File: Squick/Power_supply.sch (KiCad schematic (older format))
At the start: 17 parts, among them J10 D24V3F-5V, J9 BATT, Q1 Q_PMOS_GSD, SW4 ON/OFF, U10 LM1117-3.3

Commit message: Fixed footprints and symbol
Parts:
- SW4: footprint Button_Switch_SMD:Tact_Switch_SMD_3x6mm -> Button_Switch_SMD:SW_SPDT_CK-JS102011SAQN
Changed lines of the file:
@@
 F 0 "SW4" H 2075 6585 50  0000 C CNN
 F 1 "ON/OFF" H 2075 6494 50  0000 C CNN
-F 2 "Button_Switch_SMD:Tact_Switch_SMD_3x6mm" H 2075 6300 50  0001 C CNN
+F 2 "Button_Switch_SMD:SW_SPDT_CK-JS102011SAQN" H 2075 6300 50  0001 C CNN
 F 3 "~" H 2075 6300 50  0001 C CNN
 	1    2075 6300

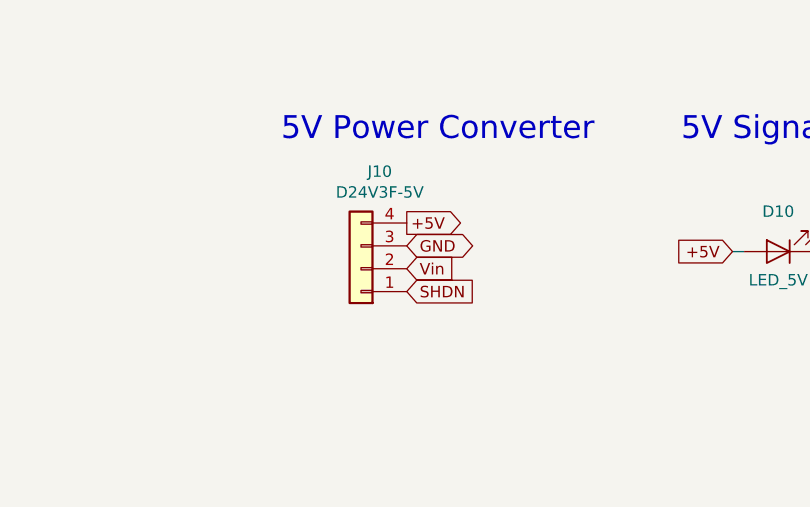
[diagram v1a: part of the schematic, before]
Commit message: Progress with PCB and some footprint debugs
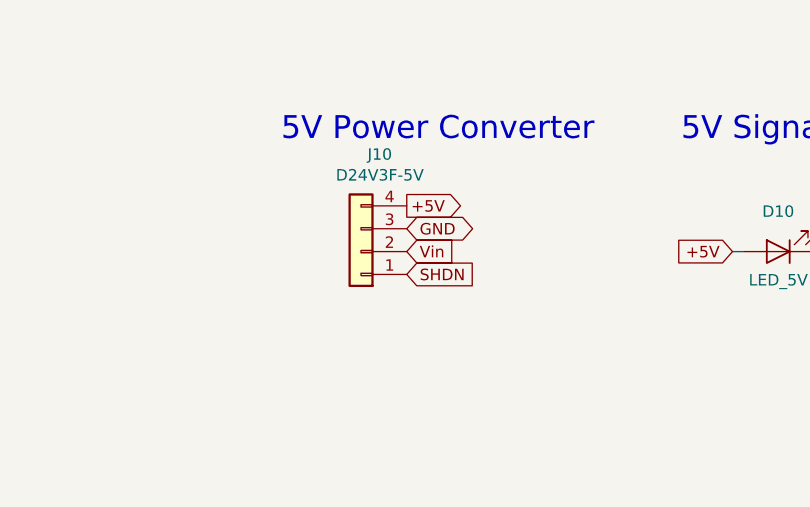
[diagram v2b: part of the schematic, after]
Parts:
- J10: footprint Connector_PinSocket_2.54mm:PinSocket_1x02_P2.54mm_Vertical -> Connector_PinSocket_2.54mm:PinSocket_1x04_P2.54mm_Vertical
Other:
- moved on the sheet: J10
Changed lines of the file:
@@
 	1    0    0    -1
 $EndComp
-Text GLabel 7100 2275 2    50   Input ~ 0
+Text GLabel 7100 2200 2    50   Input ~ 0
 SHDN
-Text GLabel 7100 2175 2    50   Input ~ 0
+Text GLabel 7100 2100 2    50   Input ~ 0
 Vin
-Text GLabel 7100 2075 2    50   BiDi ~ 0
+Text GLabel 7100 2000 2    50   BiDi ~ 0
 GND
 $Comp
 L Connector_Generic:Conn_01x04 J?
 U 1 1 60828861
-P 6900 2175
+P 6900 2100
 AR Path="/60828861" Ref="J?"  Part="1"
 AR Path="/608248A8/60828861" Ref="J10"  Part="1"
-F 0 "J10" H 6818 1750 50  0000 C CNN
-F 1 "D24V3F-5V" H 6818 1841 50  0000 C CNN
-F 2 "Connector_PinSocket_2.54mm:PinSocket_1x02_P2.54mm_Vertical" H 6900 2175 50  0001 C CNN
-F 3 "~" H 6900 2175 50  0001 C CNN
-	1    6900 2175
+F 0 "J10" H 6818 1675 50  0000 C CNN
+F 1 "D24V3F-5V" H 6818 1766 50  0000 C CNN
+F 2 "Connector_PinSocket_2.54mm:PinSocket_1x04_P2.54mm_Vertical" H 6900 2100 50  0001 C CNN
+F 3 "~" H 6900 2100 50  0001 C CNN
+	1    6900 2100
 	-1   0    0    1
 $EndComp
@@
 Wire Wire Line
 	2775 5525 2775 5625
-Text GLabel 7100 1975 2    50   Output ~ 0
+Text GLabel 7100 1900 2    50   Output ~ 0
 +5V
 $Comp

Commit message: Major progress with PCB design
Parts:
- C23, C26: footprint Capacitor_SMD:C_Elec_4x5.4 -> Capacitor_SMD:C_0603_1608Metric
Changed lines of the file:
@@
 F 0 "C23" H 6265 4796 50  0000 L CNN
 F 1 "100n" H 6265 4705 50  0000 L CNN
-F 2 "Capacitor_SMD:C_Elec_4x5.4" H 6188 4600 50  0001 C CNN
+F 2 "Capacitor_SMD:C_0603_1608Metric" H 6188 4600 50  0001 C CNN
 F 3 "~" H 6150 4750 50  0001 C CNN
 	1    6150 4750
@@
 F 0 "C26" H 8115 4771 50  0000 L CNN
 F 1 "100n" H 8115 4680 50  0000 L CNN
-F 2 "Capacitor_SMD:C_Elec_4x5.4" H 8038 4575 50  0001 C CNN
+F 2 "Capacitor_SMD:C_0603_1608Metric" H 8038 4575 50  0001 C CNN
 F 3 "~" H 8000 4725 50  0001 C CNN
 	1    8000 4725

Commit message: PCB project almost finished (without connections)
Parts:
- Q1: footprint (none) -> Package_TO_SOT_SMD:SOT-23
- R28: value 1.5k -> 10k; footprint Resistor_SMD:R_0805_2012Metric -> (none)
- SW4: value ON/OFF -> SW_SPDT; footprint Button_Switch_SMD:SW_SPDT_CK-JS102011SAQN -> (none)
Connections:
- net GND: now also R28.2; no longer R28.1
- net at Q1.1 (G): now also R28.1; no longer R28.2
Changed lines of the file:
@@
 $EndComp
-$Comp
-L Switch:SW_SPDT SW?
-U 1 1 60828874
-P 2075 6300
-AR Path="/60828874" Ref="SW?"  Part="1"
-AR Path="/608248A8/60828874" Ref="SW4"  Part="1"
-F 0 "SW4" H 2075 6585 50  0000 C CNN
-F 1 "ON/OFF" H 2075 6494 50  0000 C CNN
-F 2 "Button_Switch_SMD:SW_SPDT_CK-JS102011SAQN" H 2075 6300 50  0001 C CNN
-F 3 "~" H 2075 6300 50  0001 C CNN
-	1    2075 6300
-	-1   0    0    -1
-$EndComp
-$Comp
-L Device:Q_PMOS_GSD Q?
-U 1 1 6082887A
-P 2775 6200
-AR Path="/6082887A" Ref="Q?"  Part="1"
-AR Path="/608248A8/6082887A" Ref="Q1"  Part="1"
-F 0 "Q1" V 3024 6200 50  0000 C CNN
-F 1 "Q_PMOS_GSD" V 3115 6200 50  0000 C CNN
-F 2 "" H 2975 6300 50  0001 C CNN
-F 3 "~" H 2775 6200 50  0001 C CNN
-	1    2775 6200
-	0    -1   1    0
-$EndComp
-$Comp
-L power:VCC #PWR?
-U 1 1 60828880
-P 1850 6100
-AR Path="/60828880" Ref="#PWR?"  Part="1"
-AR Path="/608248A8/60828880" Ref="#PWR049"  Part="1"
-F 0 "#PWR049" H 1850 5950 50  0001 C CNN
-F 1 "VCC" H 1867 6273 50  0000 C CNN
-F 2 "" H 1850 6100 50  0001 C CNN
-F 3 "" H 1850 6100 50  0001 C CNN
-	1    1850 6100
-	1    0    0    -1
-$EndComp
-Wire Wire Line
-	1850 6100 1850 6200
-Wire Wire Line
-	1850 6200 1875 6200
-Wire Wire Line
-	2275 6300 2375 6300
-Wire Wire Line
-	1875 6400 1875 6525
-Wire Wire Line
-	1875 6525 2375 6525
-Wire Wire Line
-	2375 6525 2375 6300
-Connection ~ 2375 6300
-Wire Wire Line
-	2375 6300 2575 6300
-Wire Wire Line
-	2975 6300 3100 6300
-Text GLabel 3100 6300 2    50   Output ~ 0
-Vin
 $Comp
 L power:GND #PWR?
@@
 Text GLabel 2925 1750 1    50   BiDi ~ 0
 GND
-$Comp
-L Device:R R?
-U 1 1 6082889E
-P 2775 5775
-AR Path="/6082889E" Ref="R?"  Part="1"
-AR Path="/608248A8/6082889E" Ref="R28"  Part="1"
-F 0 "R28" H 2845 5821 50  0000 L CNN
-F 1 "1.5k" H 2845 5730 50  0000 L CNN
-F 2 "Resistor_SMD:R_0805_2012Metric" V 2705 5775 50  0001 C CNN
-F 3 "~" H 2775 5775 50  0001 C CNN
-	1    2775 5775
-	1    0    0    -1
-$EndComp
-Wire Wire Line
-	2775 5925 2775 6000
-Text GLabel 2775 5525 2    50   BiDi ~ 0
-GND
-Wire Wire Line
-	2775 5525 2775 5625
 Text GLabel 7100 1900 2    50   Output ~ 0
 +5V
@@
 Text Notes 2000 3150 0    100  ~ 0
 Battery Level Probe
+$Comp
+L Device:Q_PMOS_GSD Q1
+U 1 1 6056C3F2
+P 3050 6000
+F 0 "Q1" V 3393 6000 50  0000 C CNN
+F 1 "Q_PMOS_GSD" V 3302 6000 50  0000 C CNN
+F 2 "Package_TO_SOT_SMD:SOT-23" H 3250 6100 50  0001 C CNN
+F 3 "~" H 3050 6000 50  0001 C CNN
+	1    3050 6000
+	0    -1   -1   0
+$EndComp
+Text GLabel 2750 6600 0    50   BiDi ~ 0
+GND
+Text GLabel 3450 5900 2    50   Output ~ 0
+Vin
+Wire Wire Line
+	3050 6250 3050 6200
+Wire Wire Line
+	3050 6600 3050 6550
+Wire Wire Line
+	2750 6600 3050 6600
+Wire Wire Line
+	3250 5900 3450 5900
+$Comp
+L Device:R R28
+U 1 1 6056C745
+P 3050 6400
+F 0 "R28" H 3120 6446 50  0000 L CNN
+F 1 "10k" H 3120 6355 50  0000 L CNN
+F 2 "" V 2980 6400 50  0001 C CNN
+F 3 "~" H 3050 6400 50  0001 C CNN
+	1    3050 6400
+	1    0    0    -1
+$EndComp
+$Comp
+L Switch:SW_SPDT SW4
+U 1 1 60586DF8
+P 2550 5900
+F 0 "SW4" H 2550 5575 50  0000 C CNN
+F 1 "SW_SPDT" H 2550 5666 50  0000 C CNN
+F 2 "" H 2550 5900 50  0001 C CNN
+F 3 "" H 2550 5900 50  0001 C CNN
+	1    2550 5900
+	-1   0    0    1
+$EndComp
+Wire Wire Line
+	2850 5900 2750 5900
+$Comp
+L power:VCC #PWR0101
+U 1 1 60587CA7
+P 2250 5950
+F 0 "#PWR0101" H 2250 5800 50  0001 C CNN
+F 1 "VCC" H 2267 6123 50  0000 C CNN
+F 2 "" H 2250 5950 50  0001 C CNN
+F 3 "" H 2250 5950 50  0001 C CNN
+	1    2250 5950
+	1    0    0    -1
+$EndComp
+Wire Wire Line
+	2350 5800 2350 5750
+Wire Wire Line
+	2350 5750 2750 5750
+Wire Wire Line
+	2750 5750 2750 5900
+Connection ~ 2750 5900
+Wire Wire Line
+	2350 6000 2250 6000
+Wire Wire Line
+	2250 6000 2250 5950
 $EndSCHEMATC

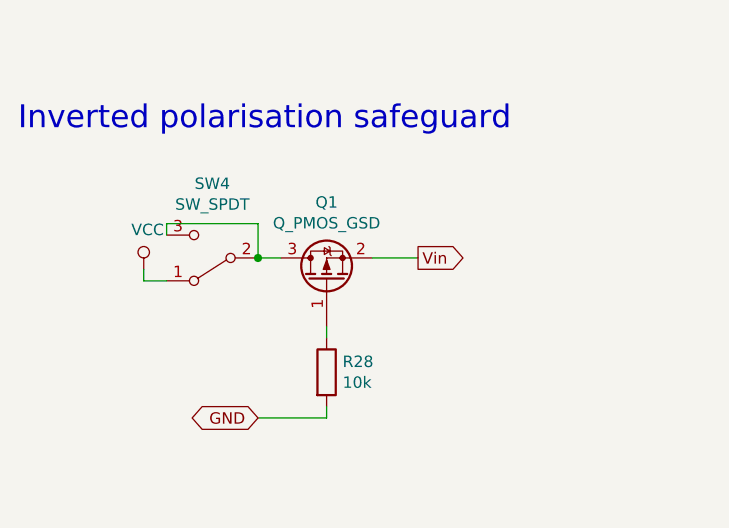
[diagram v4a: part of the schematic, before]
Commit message: Changed IMU and assigned 0603 footprints
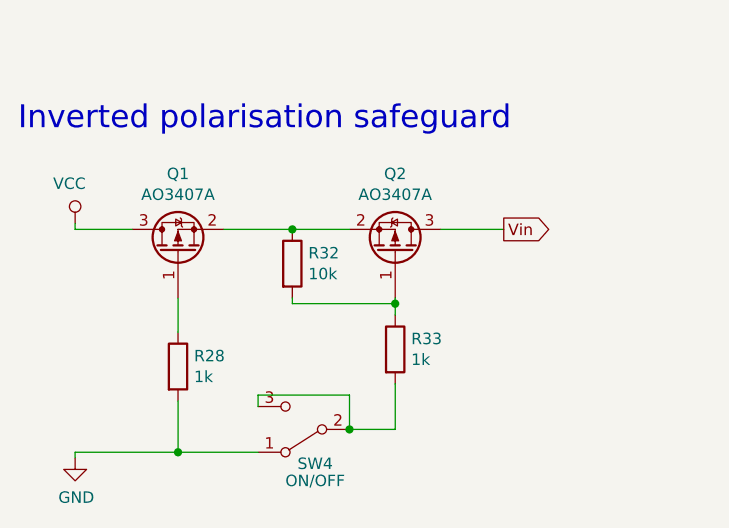
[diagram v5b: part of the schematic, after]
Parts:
- added Q2: AO3407A, Package_TO_SOT_SMD:SOT-23_Handsoldering, symbol Device:Q_PMOS_GSD
- added R32: 10k, Resistor_SMD:R_0603_1608Metric_Pad1.05x0.95mm_HandSolder, symbol Device:R
- added R33: 1k, Resistor_SMD:R_0603_1608Metric_Pad1.05x0.95mm_HandSolder, symbol Device:R
- C22: footprint Capacitor_SMD:C_0805_2012Metric -> Capacitor_SMD:C_0603_1608Metric_Pad1.05x0.95mm_HandSolder
- C23, C26: footprint Capacitor_SMD:C_0603_1608Metric -> Capacitor_SMD:C_0603_1608Metric_Pad1.05x0.95mm_HandSolder
- C24, C25: footprint Capacitor_SMD:CP_Elec_5x5.4 -> Capacitor_Tantalum_SMD:CP_EIA-3216-18_Kemet-A_Pad1.58x1.35mm_HandSolder
- D10, D11: footprint LED_SMD:LED_0805_2012Metric -> LED_SMD:LED_0603_1608Metric_Pad1.05x0.95mm_HandSolder
- Q1: value Q_PMOS_GSD -> AO3407A; footprint Package_TO_SOT_SMD:SOT-23 -> Package_TO_SOT_SMD:SOT-23_Handsoldering
- R27, R29, R30, R31: footprint Resistor_SMD:R_0805_2012Metric -> Resistor_SMD:R_0603_1608Metric_Pad1.05x0.95mm_HandSolder
- R28: value 10k -> 1k; footprint (none) -> Resistor_SMD:R_0603_1608Metric_Pad1.05x0.95mm_HandSolder
- SW4: value SW_SPDT -> ON/OFF; footprint (none) -> Connector_PinSocket_2.54mm:PinSocket_1x03_P2.54mm_Vertical
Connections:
- net GND: now also SW4.1 (A)
- net VCC: now also Q1.3 (D); no longer SW4.1 (A)
- net Vin: now also Q2.3 (D); no longer Q1.2 (S)
- net at SW4.2 (B), SW4.3 (C): now also R33.2; no longer Q1.3 (D)
- new net: Q1.2 (S), Q2.2 (S), R32.1
- new net: Q2.1 (G), R32.2, R33.1
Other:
- moved on the sheet: Q1, R28, SW4
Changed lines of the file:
@@
 EESchema Schematic File Version 4
-LIBS:Squick-cache
-EELAYER 26 0
+EELAYER 30 0
 EELAYER END
 $Descr A4 11693 8268
@@
 F 0 "C23" H 6265 4796 50  0000 L CNN
 F 1 "100n" H 6265 4705 50  0000 L CNN
-F 2 "Capacitor_SMD:C_0603_1608Metric" H 6188 4600 50  0001 C CNN
+F 2 "Capacitor_SMD:C_0603_1608Metric_Pad1.05x0.95mm_HandSolder" H 6188 4600 50  0001 C CNN
 F 3 "~" H 6150 4750 50  0001 C CNN
 	1    6150 4750
@@
 F 0 "C26" H 8115 4771 50  0000 L CNN
 F 1 "100n" H 8115 4680 50  0000 L CNN
-F 2 "Capacitor_SMD:C_0603_1608Metric" H 8038 4575 50  0001 C CNN
+F 2 "Capacitor_SMD:C_0603_1608Metric_Pad1.05x0.95mm_HandSolder" H 8038 4575 50  0001 C CNN
 F 3 "~" H 8000 4725 50  0001 C CNN
 	1    8000 4725
@@
 F 0 "C24" H 6668 4771 50  0000 L CNN
 F 1 "10u" H 6668 4680 50  0000 L CNN
-F 2 "Capacitor_SMD:CP_Elec_5x5.4" H 6588 4575 50  0001 C CNN
+F 2 "Capacitor_Tantalum_SMD:CP_EIA-3216-18_Kemet-A_Pad1.58x1.35mm_HandSolder" H 6588 4575 50  0001 C CNN
 F 3 "~" H 6550 4725 50  0001 C CNN
 	1    6550 4725
@@
 F 0 "C25" H 7693 4771 50  0000 L CNN
 F 1 "10u" H 7693 4680 50  0000 L CNN
-F 2 "Capacitor_SMD:CP_Elec_5x5.4" H 7613 4575 50  0001 C CNN
+F 2 "Capacitor_Tantalum_SMD:CP_EIA-3216-18_Kemet-A_Pad1.58x1.35mm_HandSolder" H 7613 4575 50  0001 C CNN
 F 3 "~" H 7575 4725 50  0001 C CNN
 	1    7575 4725
@@
 F 0 "R27" V 2143 3525 50  0000 C CNN
 F 1 "100k" V 2234 3525 50  0000 C CNN
-F 2 "Resistor_SMD:R_0805_2012Metric" V 2280 3525 50  0001 C CNN
+F 2 "Resistor_SMD:R_0603_1608Metric_Pad1.05x0.95mm_HandSolder" V 2280 3525 50  0001 C CNN
 F 3 "~" H 2350 3525 50  0001 C CNN
 	1    2350 3525
@@
 F 0 "R29" V 2768 3525 50  0000 C CNN
 F 1 "47k" V 2859 3525 50  0000 C CNN
-F 2 "Resistor_SMD:R_0805_2012Metric" V 2905 3525 50  0001 C CNN
+F 2 "Resistor_SMD:R_0603_1608Metric_Pad1.05x0.95mm_HandSolder" V 2905 3525 50  0001 C CNN
 F 3 "~" H 2975 3525 50  0001 C CNN
 	1    2975 3525
@@
 F 0 "D11" H 9375 4500 50  0000 C CNN
 F 1 "LED_3.3V" H 9375 4800 50  0000 C CNN
-F 2 "LED_SMD:LED_0805_2012Metric" H 9375 4675 50  0001 C CNN
+F 2 "LED_SMD:LED_0603_1608Metric_Pad1.05x0.95mm_HandSolder" H 9375 4675 50  0001 C CNN
 F 3 "~" H 9375 4675 50  0001 C CNN
 	1    9375 4675
@@
 F 0 "R31" V 9493 4675 50  0000 C CNN
 F 1 "330" V 9584 4675 50  0000 C CNN
-F 2 "Resistor_SMD:R_0805_2012Metric" V 9630 4675 50  0001 C CNN
+F 2 "Resistor_SMD:R_0603_1608Metric_Pad1.05x0.95mm_HandSolder" V 9630 4675 50  0001 C CNN
 F 3 "~" H 9700 4675 50  0001 C CNN
 	1    9700 4675
@@
 F 0 "D10" H 8725 1925 50  0000 C CNN
 F 1 "LED_5V" H 8725 2225 50  0000 C CNN
-F 2 "LED_SMD:LED_0805_2012Metric" H 8725 2100 50  0001 C CNN
+F 2 "LED_SMD:LED_0603_1608Metric_Pad1.05x0.95mm_HandSolder" H 8725 2100 50  0001 C CNN
 F 3 "~" H 8725 2100 50  0001 C CNN
 	1    8725 2100
@@
 F 0 "R30" V 8843 2100 50  0000 C CNN
 F 1 "470" V 8934 2100 50  0000 C CNN
-F 2 "Resistor_SMD:R_0805_2012Metric" V 8980 2100 50  0001 C CNN
+F 2 "Resistor_SMD:R_0603_1608Metric_Pad1.05x0.95mm_HandSolder" V 8980 2100 50  0001 C CNN
 F 3 "~" H 9050 2100 50  0001 C CNN
 	1    9050 2100
@@
 F 0 "C22" V 2900 3600 50  0000 L CNN
 F 1 "100n" V 3100 3675 50  0000 L CNN
-F 2 "Capacitor_SMD:C_0805_2012Metric" H 2975 3750 50  0001 C CNN
+F 2 "Capacitor_SMD:C_0603_1608Metric_Pad1.05x0.95mm_HandSolder" H 2975 3750 50  0001 C CNN
 F 3 "~" H 2975 3750 50  0001 C CNN
 	1    2975 3750
@@
 L Device:Q_PMOS_GSD Q1
 U 1 1 6056C3F2
-P 3050 6000
-F 0 "Q1" V 3393 6000 50  0000 C CNN
-F 1 "Q_PMOS_GSD" V 3302 6000 50  0000 C CNN
-F 2 "Package_TO_SOT_SMD:SOT-23" H 3250 6100 50  0001 C CNN
-F 3 "~" H 3050 6000 50  0001 C CNN
-	1    3050 6000
+P 2400 5875
+F 0 "Q1" V 2743 5875 50  0000 C CNN
+F 1 "AO3407A" V 2652 5875 50  0000 C CNN
+F 2 "Package_TO_SOT_SMD:SOT-23_Handsoldering" H 2600 5975 50  0001 C CNN
+F 3 "~" H 2400 5875 50  0001 C CNN
+	1    2400 5875
 	0    -1   -1   0
 $EndComp
-Text GLabel 2750 6600 0    50   BiDi ~ 0
-GND
-Text GLabel 3450 5900 2    50   Output ~ 0
+Text GLabel 3825 5775 2    50   Output ~ 0
 Vin
-Wire Wire Line
-	3050 6250 3050 6200
-Wire Wire Line
-	3050 6600 3050 6550
-Wire Wire Line
-	2750 6600 3050 6600
-Wire Wire Line
-	3250 5900 3450 5900
 $Comp
 L Device:R R28
 U 1 1 6056C745
-P 3050 6400
-F 0 "R28" H 3120 6446 50  0000 L CNN
-F 1 "10k" H 3120 6355 50  0000 L CNN
-F 2 "" V 2980 6400 50  0001 C CNN
-F 3 "~" H 3050 6400 50  0001 C CNN
-	1    3050 6400
+P 2400 6375
+F 0 "R28" H 2470 6421 50  0000 L CNN
+F 1 "1k" H 2470 6330 50  0000 L CNN
+F 2 "Resistor_SMD:R_0603_1608Metric_Pad1.05x0.95mm_HandSolder" V 2330 6375 50  0001 C CNN
+F 3 "~" H 2400 6375 50  0001 C CNN
+	1    2400 6375
 	1    0    0    -1
 $EndComp
@@
 L Switch:SW_SPDT SW4
 U 1 1 60586DF8
-P 2550 5900
-F 0 "SW4" H 2550 5575 50  0000 C CNN
-F 1 "SW_SPDT" H 2550 5666 50  0000 C CNN
-F 2 "" H 2550 5900 50  0001 C CNN
-F 3 "" H 2550 5900 50  0001 C CNN
-	1    2550 5900
+P 2950 6650
+F 0 "SW4" H 2900 6800 50  0000 C CNN
+F 1 "ON/OFF" H 2900 6875 50  0000 C CNN
+F 2 "Connector_PinSocket_2.54mm:PinSocket_1x03_P2.54mm_Vertical" H 2950 6650 50  0001 C CNN
+F 3 "" H 2950 6650 50  0001 C CNN
+	1    2950 6650
 	-1   0    0    1
 $EndComp
-Wire Wire Line
-	2850 5900 2750 5900
 $Comp
 L power:VCC #PWR0101
 U 1 1 60587CA7
-P 2250 5950
-F 0 "#PWR0101" H 2250 5800 50  0001 C CNN
-F 1 "VCC" H 2267 6123 50  0000 C CNN
-F 2 "" H 2250 5950 50  0001 C CNN
-F 3 "" H 2250 5950 50  0001 C CNN
-	1    2250 5950
-	1    0    0    -1
-$EndComp
-Wire Wire Line
-	2350 5800 2350 5750
-Wire Wire Line
-	2350 5750 2750 5750
-Wire Wire Line
-	2750 5750 2750 5900
-Connection ~ 2750 5900
-Wire Wire Line
-	2350 6000 2250 6000
-Wire Wire Line
-	2250 6000 2250 5950
+P 1950 5750
+F 0 "#PWR0101" H 1950 5600 50  0001 C CNN
+F 1 "VCC" H 1925 5925 50  0000 C CNN
+F 2 "" H 1950 5750 50  0001 C CNN
+F 3 "" H 1950 5750 50  0001 C CNN
+	1    1950 5750
+	1    0    0    -1
+$EndComp
+Wire Wire Line
+	2750 6550 2750 6500
+Wire Wire Line
+	2750 6500 3150 6500
+Wire Wire Line
+	3150 6500 3150 6650
+Connection ~ 3150 6650
+$Comp
+L Device:Q_PMOS_GSD Q2
+U 1 1 60575C25
+P 3350 5875
+F 0 "Q2" V 3693 5875 50  0000 C CNN
+F 1 "AO3407A" V 3602 5875 50  0000 C CNN
+F 2 "Package_TO_SOT_SMD:SOT-23_Handsoldering" H 3550 5975 50  0001 C CNN
+F 3 "~" H 3350 5875 50  0001 C CNN
+	1    3350 5875
+	0    1    -1   0
+$EndComp
+Wire Wire Line
+	2600 5775 2900 5775
+Wire Wire Line
+	3150 6650 3350 6650
+Wire Wire Line
+	2400 6750 2750 6750
+$Comp
+L Device:R R32
+U 1 1 6057DE5E
+P 2900 5925
+F 0 "R32" H 2970 5971 50  0000 L CNN
+F 1 "10k" H 2970 5880 50  0000 L CNN
+F 2 "Resistor_SMD:R_0603_1608Metric_Pad1.05x0.95mm_HandSolder" V 2830 5925 50  0001 C CNN
+F 3 "~" H 2900 5925 50  0001 C CNN
+	1    2900 5925
+	1    0    0    -1
+$EndComp
+$Comp
+L Device:R R33
+U 1 1 6057E3E0
+P 3350 6300
+F 0 "R33" H 3420 6346 50  0000 L CNN
+F 1 "1k" H 3420 6255 50  0000 L CNN
+F 2 "Resistor_SMD:R_0603_1608Metric_Pad1.05x0.95mm_HandSolder" V 3280 6300 50  0001 C CNN
+F 3 "~" H 3350 6300 50  0001 C CNN
+	1    3350 6300
+	1    0    0    -1
+$EndComp
+Connection ~ 2900 5775
+Wire Wire Line
+	2900 5775 3150 5775
+Connection ~ 2400 6750
+Wire Wire Line
+	2400 6525 2400 6750
+Wire Wire Line
+	2400 6075 2400 6225
+Wire Wire Line
+	1950 5750 1950 5775
+Wire Wire Line
+	1950 5775 2200 5775
+Wire Wire Line
+	2900 6075 2900 6100
+Wire Wire Line
+	2900 6100 3350 6100
+Wire Wire Line
+	3350 6100 3350 6075
+Wire Wire Line
+	3350 6100 3350 6150
+Connection ~ 3350 6100
+Wire Wire Line
+	3350 6450 3350 6650
+$Comp
+L power:GND #PWR0102
+U 1 1 60588E84
+P 1950 6775
+F 0 "#PWR0102" H 1950 6525 50  0001 C CNN
+F 1 "GND" H 1955 6602 50  0000 C CNN
+F 2 "" H 1950 6775 50  0001 C CNN
+F 3 "" H 1950 6775 50  0001 C CNN
+	1    1950 6775
+	1    0    0    -1
+$EndComp
+Wire Wire Line
+	1950 6750 1950 6775
+Wire Wire Line
+	1950 6750 2400 6750
+Wire Wire Line
+	3550 5775 3825 5775
 $EndSCHEMATC
